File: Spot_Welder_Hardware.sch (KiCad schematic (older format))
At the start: 147 parts, among them J1 Mini USB, J2 Conn_01x03_Male, Q1 Q_NMOS_GSD, Q10 Q_NMOS_GDS, Q11 Q_NMOS_GDS, Q12 Q_NMOS_GDS, Q13 Q_NMOS_GDS, Q2 2N2219, Q3 Q_NMOS_GDS, Q4 Q_NMOS_GDS, Q5 Q_NMOS_GDS, Q6 Q_NMOS_GDS, Q7 Q_NMOS_GDS, Q8 Q_NMOS_GDS, Q9 Q_NMOS_GDS, SW1 SW_Push, SW2 SW_SPDT, SW3 Lead Voltage Trigger, SW4 SW_Push, U1 OKI, U2 ATMEGA328P, U3 FAN3122TMXCT-ND, U4 FT232RL, U5 FAN3122TMXCT-ND, Y1 Crystal

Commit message: Modified OverVoltage Protection LED
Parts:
- added R?: 10K, Resistors_SMD:R_0603_HandSoldering, symbol Device:R
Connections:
- wire segments 324 -> 328
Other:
- moved on the sheet: D11
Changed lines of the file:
@@
 L Device:LED D11
 U 1 1 5B37E14A
-P 8900 3300
-F 0 "D11" H 8900 3400 50  0000 C CNN
-F 1 "Over Voltage" H 8900 3200 50  0000 C CNN
-F 2 "LEDs:LED_0603_HandSoldering" H 8900 3300 50  0001 C CNN
-F 3 "" H 8900 3300 50  0001 C CNN
-	1    8900 3300
-	0    -1   -1   0
+P 8150 2450
+F 0 "D11" H 8150 2550 50  0000 C CNN
+F 1 "Over Voltage" H 8150 2350 50  0000 C CNN
+F 2 "LEDs:LED_0603_HandSoldering" H 8150 2450 50  0001 C CNN
+F 3 "" H 8150 2450 50  0001 C CNN
+	1    8150 2450
+	-1   0    0    1
 $EndComp
 Text Notes 6850 2600 0    24   ~ 0
@@
 	9000 2700 8900 2700
 Wire Wire Line
-	9300 3450 8900 3450
-Wire Wire Line
 	8200 3100 8150 3100
 Wire Wire Line
 	8150 3100 8150 3450
 Connection ~ 8150 3450
-Connection ~ 8900 3450
 Text Label 14350 5750 0    60   ~ 0
 DTR
@@
 	8150 3450 7800 3450
 Wire Wire Line
-	8900 3450 8150 3450
-Wire Wire Line
 	7950 3850 7950 3700
 Wire Wire Line
@@
 Text GLabel 5600 5750 0    60   Input ~ 0
 +5V
+$Comp
+L Device:R R?
+U 1 1 5BB1B4E9
+P 8650 2450
+F 0 "R?" V 8730 2450 50  0000 C CNN
+F 1 "10K" V 8650 2450 50  0000 C CNN
+F 2 "Resistors_SMD:R_0603_HandSoldering" V 8580 2450 50  0001 C CNN
+F 3 "" H 8650 2450 50  0001 C CNN
+	1    8650 2450
+	0    1    1    0
+$EndComp
+Wire Wire Line
+	8900 2600 8900 2450
+Wire Wire Line
+	8900 2450 8800 2450
+Wire Wire Line
+	8150 3450 9300 3450
+Connection ~ 8900 2600
+Wire Wire Line
+	8500 2450 8300 2450
+Wire Wire Line
+	8000 2450 7850 2450
+Wire Wire Line
+	7850 2450 7850 2600
 $EndSCHEMATC

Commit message: Swapped main MOSFETs to PSMN1R1-30PL
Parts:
- Q10, Q11, Q12, Q13, Q4, Q5, Q6, Q7, Q8, Q9: Part Number PSMN2R0-30PL -> PSMN1R1
- gave numbers to parts that had none: 1
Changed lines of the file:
@@
 F 2 "TO_SOT_Packages_THT:TO-220-3_Vertical" H 10650 2850 50  0001 C CNN
 F 3 "" H 10450 2750 50  0001 C CNN
-F 4 "PSMN2R0-30PL" H 10450 2750 60  0001 C CNN "Part Number"
+F 4 "PSMN1R1" H 10450 2750 60  0001 C CNN "Part Number"
 	1    10450 2750
-	1    0    0    -1
-$EndComp
-$Comp
-L Device:Q_NMOS_GDS Q5
-U 1 1 5B2DEBF2
-P 10950 2750
-F 0 "Q5" H 11150 2800 50  0000 L CNN
-F 1 "Q_NMOS_GDS" H 11150 2700 50  0001 L CNN
-F 2 "TO_SOT_Packages_THT:TO-220-3_Vertical" H 11150 2850 50  0001 C CNN
-F 3 "" H 10950 2750 50  0001 C CNN
-F 4 "PSMN2R0-30PL" H 10950 2750 60  0001 C CNN "Part Number"
-	1    10950 2750
-	1    0    0    -1
-$EndComp
-$Comp
-L Device:Q_NMOS_GDS Q6
-U 1 1 5B2DED1C
-P 11450 2750
-F 0 "Q6" H 11650 2800 50  0000 L CNN
-F 1 "Q_NMOS_GDS" H 11650 2700 50  0001 L CNN
-F 2 "TO_SOT_Packages_THT:TO-220-3_Vertical" H 11650 2850 50  0001 C CNN
-F 3 "" H 11450 2750 50  0001 C CNN
-F 4 "PSMN2R0-30PL" H 11450 2750 60  0001 C CNN "Part Number"
-	1    11450 2750
-	1    0    0    -1
-$EndComp
-$Comp
-L Device:Q_NMOS_GDS Q7
-U 1 1 5B2DEDBF
-P 11950 2750
-F 0 "Q7" H 12150 2800 50  0000 L CNN
-F 1 "Q_NMOS_GDS" H 12150 2700 50  0001 L CNN
-F 2 "TO_SOT_Packages_THT:TO-220-3_Vertical" H 12150 2850 50  0001 C CNN
-F 3 "" H 11950 2750 50  0001 C CNN
-F 4 "PSMN2R0-30PL" H 11950 2750 60  0001 C CNN "Part Number"
-	1    11950 2750
-	1    0    0    -1
-$EndComp
-$Comp
-L Device:Q_NMOS_GDS Q8
-U 1 1 5B2DEEC5
-P 12450 2750
-F 0 "Q8" H 12650 2800 50  0000 L CNN
-F 1 "Q_NMOS_GDS" H 12650 2700 50  0001 L CNN
-F 2 "TO_SOT_Packages_THT:TO-220-3_Vertical" H 12650 2850 50  0001 C CNN
-F 3 "" H 12450 2750 50  0001 C CNN
-F 4 "PSMN2R0-30PL" H 12450 2750 60  0001 C CNN "Part Number"
-	1    12450 2750
-	1    0    0    -1
-$EndComp
-$Comp
-L Device:Q_NMOS_GDS Q9
-U 1 1 5B2DF0C1
-P 12950 2750
-F 0 "Q9" H 13150 2800 50  0000 L CNN
-F 1 "Q_NMOS_GDS" H 13150 2700 50  0001 L CNN
-F 2 "TO_SOT_Packages_THT:TO-220-3_Vertical" H 13150 2850 50  0001 C CNN
-F 3 "" H 12950 2750 50  0001 C CNN
-F 4 "PSMN2R0-30PL" H 12950 2750 60  0001 C CNN "Part Number"
-	1    12950 2750
-	1    0    0    -1
-$EndComp
-$Comp
-L Device:Q_NMOS_GDS Q10
-U 1 1 5B2DF0C8
-P 13450 2750
-F 0 "Q10" H 13650 2800 50  0000 L CNN
-F 1 "Q_NMOS_GDS" H 13650 2700 50  0001 L CNN
-F 2 "TO_SOT_Packages_THT:TO-220-3_Vertical" H 13650 2850 50  0001 C CNN
-F 3 "" H 13450 2750 50  0001 C CNN
-F 4 "PSMN2R0-30PL" H 13450 2750 60  0001 C CNN "Part Number"
-	1    13450 2750
-	1    0    0    -1
-$EndComp
-$Comp
-L Device:Q_NMOS_GDS Q11
-U 1 1 5B2DF0CF
-P 13950 2750
-F 0 "Q11" H 14150 2800 50  0000 L CNN
-F 1 "Q_NMOS_GDS" H 14150 2700 50  0001 L CNN
-F 2 "TO_SOT_Packages_THT:TO-220-3_Vertical" H 14150 2850 50  0001 C CNN
-F 3 "" H 13950 2750 50  0001 C CNN
-F 4 "PSMN2R0-30PL" H 13950 2750 60  0001 C CNN "Part Number"
-	1    13950 2750
-	1    0    0    -1
-$EndComp
-$Comp
-L Device:Q_NMOS_GDS Q12
-U 1 1 5B2DF0D6
-P 14450 2750
-F 0 "Q12" H 14650 2800 50  0000 L CNN
-F 1 "Q_NMOS_GDS" H 14650 2700 50  0001 L CNN
-F 2 "TO_SOT_Packages_THT:TO-220-3_Vertical" H 14650 2850 50  0001 C CNN
-F 3 "" H 14450 2750 50  0001 C CNN
-F 4 "PSMN2R0-30PL" H 14450 2750 60  0001 C CNN "Part Number"
-	1    14450 2750
-	1    0    0    -1
-$EndComp
-$Comp
-L Device:Q_NMOS_GDS Q13
-U 1 1 5B2DF0DD
-P 14950 2750
-F 0 "Q13" H 15150 2800 50  0000 L CNN
-F 1 "Q_NMOS_GDS" H 15150 2700 50  0001 L CNN
-F 2 "TO_SOT_Packages_THT:TO-220-3_Vertical" H 15150 2850 50  0001 C CNN
-F 3 "" H 14950 2750 50  0001 C CNN
-F 4 "PSMN2R0-30PL" H 14950 2750 60  0001 C CNN "Part Number"
-	1    14950 2750
 	1    0    0    -1
 $EndComp
@@
 Connection ~ 10550 2950
 Connection ~ 10550 2550
-Connection ~ 14550 2550
-Connection ~ 14050 2550
-Connection ~ 13550 2550
-Connection ~ 13050 2550
-Connection ~ 12550 2550
-Connection ~ 12050 2550
-Connection ~ 11550 2550
-Connection ~ 11050 2550
-Connection ~ 11050 2950
-Connection ~ 11550 2950
-Connection ~ 12050 2950
-Connection ~ 12550 2950
-Connection ~ 13050 2950
-Connection ~ 13550 2950
-Connection ~ 14050 2950
-Connection ~ 14550 2950
 Connection ~ 14250 3700
 Connection ~ 13750 3700
@@
 	10800 2250 11800 2250
 Wire Wire Line
-	10550 2950 11050 2950
-Wire Wire Line
 	10550 2550 10800 2550
 Wire Wire Line
-	14550 2550 14800 2550
-Wire Wire Line
-	14050 2550 14550 2550
-Wire Wire Line
-	13550 2550 13800 2550
-Wire Wire Line
-	13050 2550 13550 2550
-Wire Wire Line
-	12550 2550 12800 2550
-Wire Wire Line
-	12050 2550 12550 2550
-Wire Wire Line
-	11550 2550 11800 2550
-Wire Wire Line
-	11050 2550 11550 2550
-Wire Wire Line
-	11050 2950 11550 2950
-Wire Wire Line
-	11550 2950 12050 2950
-Wire Wire Line
-	12050 2950 12550 2950
-Wire Wire Line
-	12550 2950 13050 2950
-Wire Wire Line
-	13050 2950 13550 2950
-Wire Wire Line
-	13550 2950 14050 2950
-Wire Wire Line
-	14050 2950 14550 2950
-Wire Wire Line
-	14550 2950 15050 2950
-Wire Wire Line
 	14250 3700 14750 3700
 Wire Wire Line
@@
 Wire Wire Line
 	4000 3850 4200 3850
-Wire Wire Line
-	10800 2550 11050 2550
-Wire Wire Line
-	11800 2550 12050 2550
-Wire Wire Line
-	12800 2550 13050 2550
-Wire Wire Line
-	13800 2550 14050 2550
 Wire Wire Line
 	14800 2550 15050 2550
@@
 +5V
 $Comp
-L Device:R R?
+L Device:R R40
 U 1 1 5BB1B4E9
 P 8650 2450
-F 0 "R?" V 8730 2450 50  0000 C CNN
+F 0 "R40" V 8730 2450 50  0000 C CNN
 F 1 "10K" V 8650 2450 50  0000 C CNN
 F 2 "Resistors_SMD:R_0603_HandSoldering" V 8580 2450 50  0001 C CNN
@@
 Wire Wire Line
 	7850 2450 7850 2600
+Wire Wire Line
+	13800 2550 14050 2550
+Wire Wire Line
+	12800 2550 13050 2550
+Wire Wire Line
+	11800 2550 12050 2550
+Wire Wire Line
+	10800 2550 11050 2550
+Wire Wire Line
+	10550 2950 11050 2950
+$Comp
+L Device:Q_NMOS_GDS Q5
+U 1 1 5BBA7D9A
+P 10950 2750
+F 0 "Q5" H 11150 2800 50  0000 L CNN
+F 1 "Q_NMOS_GDS" H 11150 2700 50  0001 L CNN
+F 2 "TO_SOT_Packages_THT:TO-220-3_Vertical" H 11150 2850 50  0001 C CNN
+F 3 "" H 10950 2750 50  0001 C CNN
+F 4 "PSMN1R1" H 10950 2750 60  0001 C CNN "Part Number"
+	1    10950 2750
+	1    0    0    -1
+$EndComp
+Connection ~ 11050 2550
+Wire Wire Line
+	11050 2550 11550 2550
+Connection ~ 11050 2950
+Wire Wire Line
+	11050 2950 11550 2950
+$Comp
+L Device:Q_NMOS_GDS Q6
+U 1 1 5BBA7ECA
+P 11450 2750
+F 0 "Q6" H 11650 2800 50  0000 L CNN
+F 1 "Q_NMOS_GDS" H 11650 2700 50  0001 L CNN
+F 2 "TO_SOT_Packages_THT:TO-220-3_Vertical" H 11650 2850 50  0001 C CNN
+F 3 "" H 11450 2750 50  0001 C CNN
+F 4 "PSMN1R1" H 11450 2750 60  0001 C CNN "Part Number"
+	1    11450 2750
+	1    0    0    -1
+$EndComp
+Connection ~ 11550 2550
+Wire Wire Line
+	11550 2550 11800 2550
+Connection ~ 11550 2950
+Wire Wire Line
+	11550 2950 12050 2950
+$Comp
+L Device:Q_NMOS_GDS Q7
+U 1 1 5BBA8000
+P 11950 2750
+F 0 "Q7" H 12150 2800 50  0000 L CNN
+F 1 "Q_NMOS_GDS" H 12150 2700 50  0001 L CNN
+F 2 "TO_SOT_Packages_THT:TO-220-3_Vertical" H 12150 2850 50  0001 C CNN
+F 3 "" H 11950 2750 50  0001 C CNN
+F 4 "PSMN1R1" H 11950 2750 60  0001 C CNN "Part Number"
+	1    11950 2750
+	1    0    0    -1
+$EndComp
+Connection ~ 12050 2550
+Wire Wire Line
+	12050 2550 12550 2550
+Connection ~ 12050 2950
+Wire Wire Line
+	12050 2950 12550 2950
+$Comp
+L Device:Q_NMOS_GDS Q8
+U 1 1 5BBA8134
+P 12450 2750
+F 0 "Q8" H 12650 2800 50  0000 L CNN
+F 1 "Q_NMOS_GDS" H 12650 2700 50  0001 L CNN
+F 2 "TO_SOT_Packages_THT:TO-220-3_Vertical" H 12650 2850 50  0001 C CNN
+F 3 "" H 12450 2750 50  0001 C CNN
+F 4 "PSMN1R1" H 12450 2750 60  0001 C CNN "Part Number"
+	1    12450 2750
+	1    0    0    -1
+$EndComp
+Connection ~ 12550 2550
+Wire Wire Line
+	12550 2550 12800 2550
+Connection ~ 12550 2950
+Wire Wire Line
+	12550 2950 13050 2950
+$Comp
+L Device:Q_NMOS_GDS Q9
+U 1 1 5BBA826C
+P 12950 2750
+F 0 "Q9" H 13150 2800 50  0000 L CNN
+F 1 "Q_NMOS_GDS" H 13150 2700 50  0001 L CNN
+F 2 "TO_SOT_Packages_THT:TO-220-3_Vertical" H 13150 2850 50  0001 C CNN
+F 3 "" H 12950 2750 50  0001 C CNN
+F 4 "PSMN1R1" H 12950 2750 60  0001 C CNN "Part Number"
+	1    12950 2750
+	1    0    0    -1
+$EndComp
+Connection ~ 13050 2550
+Wire Wire Line
+	13050 2550 13550 2550
+Connection ~ 13050 2950
+Wire Wire Line
+	13050 2950 13550 2950
+$Comp
+L Device:Q_NMOS_GDS Q10
+U 1 1 5BBA83A4
+P 13450 2750
+F 0 "Q10" H 13650 2800 50  0000 L CNN
+F 1 "Q_NMOS_GDS" H 13650 2700 50  0001 L CNN
+F 2 "TO_SOT_Packages_THT:TO-220-3_Vertical" H 13650 2850 50  0001 C CNN
+F 3 "" H 13450 2750 50  0001 C CNN
+F 4 "PSMN1R1" H 13450 2750 60  0001 C CNN "Part Number"
+	1    13450 2750
+	1    0    0    -1
+$EndComp
+Connection ~ 13550 2550
+Wire Wire Line
+	13550 2550 13800 2550
+Connection ~ 13550 2950
+Wire Wire Line
+	13550 2950 14050 2950
+$Comp
+L Device:Q_NMOS_GDS Q11
+U 1 1 5BBA84E2
+P 13950 2750
+F 0 "Q11" H 14150 2800 50  0000 L CNN
+F 1 "Q_NMOS_GDS" H 14150 2700 50  0001 L CNN
+F 2 "TO_SOT_Packages_THT:TO-220-3_Vertical" H 14150 2850 50  0001 C CNN
+F 3 "" H 13950 2750 50  0001 C CNN
+F 4 "PSMN1R1" H 13950 2750 60  0001 C CNN "Part Number"
+	1    13950 2750
+	1    0    0    -1
+$EndComp
+Connection ~ 14050 2550
+Wire Wire Line
+	14050 2550 14550 2550
+Connection ~ 14050 2950
+Wire Wire Line
+	14050 2950 14550 2950
+$Comp
+L Device:Q_NMOS_GDS Q12
+U 1 1 5BBA8620
+P 14450 2750
+F 0 "Q12" H 14650 2800 50  0000 L CNN
+F 1 "Q_NMOS_GDS" H 14650 2700 50  0001 L CNN
+F 2 "TO_SOT_Packages_THT:TO-220-3_Vertical" H 14650 2850 50  0001 C CNN
+F 3 "" H 14450 2750 50  0001 C CNN
+F 4 "PSMN1R1" H 14450 2750 60  0001 C CNN "Part Number"
+	1    14450 2750
+	1    0    0    -1
+$EndComp
+Connection ~ 14550 2550
+Wire Wire Line
+	14550 2550 14800 2550
+Connection ~ 14550 2950
+Wire Wire Line
+	14550 2950 15050 2950
+$Comp
+L Device:Q_NMOS_GDS Q13
+U 1 1 5BBA8762
+P 14950 2750
+F 0 "Q13" H 15150 2800 50  0000 L CNN
+F 1 "Q_NMOS_GDS" H 15150 2700 50  0001 L CNN
+F 2 "TO_SOT_Packages_THT:TO-220-3_Vertical" H 15150 2850 50  0001 C CNN
+F 3 "" H 14950 2750 50  0001 C CNN
+F 4 "PSMN1R1" H 14950 2750 60  0001 C CNN "Part Number"
+	1    14950 2750
+	1    0    0    -1
+$EndComp
 $EndSCHEMATC

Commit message: Modified Analog limiter circuit for analogue reads
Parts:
- removed D8: 5V, Diodes_SMD:D_SOD-123, symbol Device:D_Zener
- removed Q3: Q_NMOS_GDS, TO_SOT_Packages_THT:TO-220-3_Vertical, symbol Device:Q_NMOS_GDS
- added D?: 5V, Diodes_SMD:D_SOD-123, symbol Device:D_Zener
- added Q?: Q_NMOS_GDS, TO_SOT_Packages_THT:TO-220-3_Vertical, symbol Device:Q_NMOS_GDS
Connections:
- wire segments 328 -> 324
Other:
- moved on the sheet: D9, R10, R11, R15, R16
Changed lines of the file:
@@
 Text Notes 5900 6500 0    60   ~ 0
 Capacitor Voltage Read
-Text GLabel 5950 6600 0    60   Input ~ 0
+Text GLabel 6200 6950 0    60   Input ~ 0
 V+
 $Comp
 L Device:R R15
 U 1 1 5B339706
-P 6100 6600
-F 0 "R15" V 6180 6600 50  0000 C CNN
-F 1 "3000" V 6100 6600 50  0000 C CNN
-F 2 "Resistors_SMD:R_0603_HandSoldering" V 6030 6600 50  0001 C CNN
-F 3 "" H 6100 6600 50  0001 C CNN
-	1    6100 6600
+P 6350 6950
+F 0 "R15" V 6430 6950 50  0000 C CNN
+F 1 "3000" V 6350 6950 50  0000 C CNN
+F 2 "Resistors_SMD:R_0603_HandSoldering" V 6280 6950 50  0001 C CNN
+F 3 "" H 6350 6950 50  0001 C CNN
+	1    6350 6950
 	0    1    1    0
 $EndComp
@@
 L Device:R R16
 U 1 1 5B339851
-P 6300 6800
-F 0 "R16" V 6380 6800 50  0000 C CNN
-F 1 "1000" V 6300 6800 50  0000 C CNN
-F 2 "Resistors_SMD:R_0603_HandSoldering" V 6230 6800 50  0001 C CNN
-F 3 "" H 6300 6800 50  0001 C CNN
-	1    6300 6800
-	1    0    0    -1
-$EndComp
-Text GLabel 5950 7050 0    60   UnSpc ~ 0
+P 6550 7150
+F 0 "R16" V 6630 7150 50  0000 C CNN
+F 1 "1000" V 6550 7150 50  0000 C CNN
+F 2 "Resistors_SMD:R_0603_HandSoldering" V 6480 7150 50  0001 C CNN
+F 3 "" H 6550 7150 50  0001 C CNN
+	1    6550 7150
+	1    0    0    -1
+$EndComp
+Text GLabel 6200 7400 0    60   UnSpc ~ 0
 GND
-Text GLabel 6800 6650 3    60   Output ~ 0
+Text GLabel 6750 7000 3    60   Output ~ 0
 V_Sense
 $Comp
 L Device:D_Zener D9
 U 1 1 5B33E128
-P 6600 6800
-F 0 "D9" H 6600 6900 50  0000 C CNN
-F 1 "5V" H 6600 6700 50  0000 C CNN
-F 2 "Diodes_SMD:D_SOD-123" H 6600 6800 50  0001 C CNN
-F 3 "" H 6600 6800 50  0001 C CNN
-F 4 "BZT52C5V1-FDICT-ND" H 6600 6800 60  0001 C CNN "Part Number"
-	1    6600 6800
-	0    1    1    0
+P 6350 6700
+F 0 "D9" H 6350 6800 50  0000 C CNN
+F 1 "5V" H 6350 6600 50  0000 C CNN
+F 2 "Diodes_SMD:D_SOD-123" H 6350 6700 50  0001 C CNN
+F 3 "" H 6350 6700 50  0001 C CNN
+F 4 "BZT52C5V1-FDICT-ND" H 6350 6700 60  0001 C CNN "Part Number"
+	1    6350 6700
+	1    0    0    -1
 $EndComp
 Text GLabel 2250 6200 0    60   Input ~ 0
@@
 	1    0    0    -1
 $EndComp
-Text Notes 4700 6500 0    60   ~ 0
+Text Notes 4500 6500 0    60   ~ 0
 Lead Voltage Read
-Text GLabel 4500 6600 0    60   Input ~ 0
+Text GLabel 4600 6950 0    60   Input ~ 0
 VS
 $Comp
 L Device:R R10
 U 1 1 5B36668A
-P 4650 6600
-F 0 "R10" V 4730 6600 50  0000 C CNN
-F 1 "3000" V 4650 6600 50  0000 C CNN
-F 2 "Resistors_SMD:R_0603_HandSoldering" V 4580 6600 50  0001 C CNN
-F 3 "" H 4650 6600 50  0001 C CNN
-	1    4650 6600
+P 4750 6950
+F 0 "R10" V 4830 6950 50  0000 C CNN
+F 1 "3000" V 4750 6950 50  0000 C CNN
+F 2 "Resistors_SMD:R_0603_HandSoldering" V 4680 6950 50  0001 C CNN
+F 3 "" H 4750 6950 50  0001 C CNN
+	1    4750 6950
 	0    1    1    0
 $EndComp
@@
 L Device:R R11
 U 1 1 5B366690
-P 4850 6800
-F 0 "R11" V 4930 6800 50  0000 C CNN
-F 1 "1000" V 4850 6800 50  0000 C CNN
-F 2 "Resistors_SMD:R_0603_HandSoldering" V 4780 6800 50  0001 C CNN
-F 3 "" H 4850 6800 50  0001 C CNN
-	1    4850 6800
-	1    0    0    -1
-$EndComp
-Text GLabel 4500 7050 0    60   UnSpc ~ 0
+P 4950 7150
+F 0 "R11" V 5030 7150 50  0000 C CNN
+F 1 "1000" V 4950 7150 50  0000 C CNN
+F 2 "Resistors_SMD:R_0603_HandSoldering" V 4880 7150 50  0001 C CNN
+F 3 "" H 4950 7150 50  0001 C CNN
+	1    4950 7150
+	1    0    0    -1
+$EndComp
+Text GLabel 4600 7400 0    60   UnSpc ~ 0
 GND
-Text GLabel 5350 6650 3    60   Output ~ 0
+Text GLabel 5150 7000 3    60   Output ~ 0
 Lead_Sense
-$Comp
-L Device:D_Zener D8
-U 1 1 5B36669B
-P 5150 6800
-F 0 "D8" H 5150 6900 50  0000 C CNN
-F 1 "5V" H 5150 6700 50  0000 C CNN
-F 2 "Diodes_SMD:D_SOD-123" H 5150 6800 50  0001 C CNN
-F 3 "" H 5150 6800 50  0001 C CNN
-F 4 "BZT52C5V1-FDICT-ND" H 5150 6800 60  0001 C CNN "Part Number"
-	1    5150 6800
-	0    1    1    0
-$EndComp
 $Comp
 L Device:R R27
@@
 Wire Wire Line
 	2150 2400 2350 2400
-Connection ~ 4850 7050
-Wire Wire Line
-	4500 7050 4850 7050
-Wire Wire Line
-	4850 6950 4850 7050
-Wire Wire Line
-	5150 7050 5150 6950
-Connection ~ 5150 6600
-Wire Wire Line
-	5150 6600 5150 6650
-Connection ~ 4850 6600
-Wire Wire Line
-	4800 6600 4850 6600
-Wire Wire Line
-	4850 6650 4850 6600
+Wire Wire Line
+	4600 7400 4950 7400
+Wire Wire Line
+	4950 7300 4950 7400
+Wire Wire Line
+	4900 6950 4950 6950
+Wire Wire Line
+	4950 7000 4950 6950
 Connection ~ 8200 4450
 Connection ~ 8200 3850
@@
 Wire Wire Line
 	2300 6200 2300 6250
-Connection ~ 6300 7050
-Wire Wire Line
-	5950 7050 6300 7050
-Wire Wire Line
-	6300 6950 6300 7050
-Wire Wire Line
-	6600 7050 6600 6950
-Connection ~ 6600 6600
-Wire Wire Line
-	6600 6600 6600 6650
-Connection ~ 6300 6600
-Wire Wire Line
-	6250 6600 6300 6600
-Wire Wire Line
-	6300 6650 6300 6600
+Wire Wire Line
+	6200 7400 6550 7400
+Wire Wire Line
+	6550 7300 6550 7400
+Wire Wire Line
+	6500 6950 6550 6950
+Wire Wire Line
+	6550 7000 6550 6950
 Wire Wire Line
 	3900 5400 3900 5500
@@
 Wire Notes Line
 	1850 7700 15300 7700
-Wire Wire Line
-	6800 6600 6800 6650
-Wire Wire Line
-	5350 6600 5350 6650
 Wire Notes Line
 	5650 6200 5650 7700
@@
 	0    1    1    0
 $EndComp
-$Comp
-L Device:Q_NMOS_GDS Q3
-U 1 1 5B3E6852
-P 9200 2950
-F 0 "Q3" H 9400 3000 50  0000 L CNN
-F 1 "Q_NMOS_GDS" H 9400 2900 50  0001 L CNN
-F 2 "TO_SOT_Packages_THT:TO-220-3_Vertical" H 9400 3050 50  0001 C CNN
-F 3 "" H 9200 2950 50  0001 C CNN
-F 4 "PSMN2R0-30PL" H 9200 2950 60  0001 C CNN "Part Number"
-	1    9200 2950
-	1    0    0    -1
-$EndComp
 Text GLabel 5700 3600 2    60   Output ~ 0
 V+
@@
 	12550 5700 12550 6250
 Wire Wire Line
-	4850 7050 5150 7050
-Wire Wire Line
-	5150 6600 5350 6600
-Wire Wire Line
-	4850 6600 5150 6600
-Wire Wire Line
 	8200 4450 9150 4450
 Wire Wire Line
 	8200 3850 8500 3850
-Wire Wire Line
-	6300 7050 6600 7050
-Wire Wire Line
-	6600 6600 6800 6600
-Wire Wire Line
-	6300 6600 6600 6600
 Wire Wire Line
 	8200 4150 8500 4150
@@
 	1    0    0    -1
 $EndComp
+$Comp
+L Device:Q_NMOS_GDS Q?
+U 1 1 5BBA9147
+P 9200 2950
+F 0 "Q?" H 9400 3000 50  0000 L CNN
+F 1 "Q_NMOS_GDS" H 9400 2900 50  0001 L CNN
+F 2 "TO_SOT_Packages_THT:TO-220-3_Vertical" H 9400 3050 50  0001 C CNN
+F 3 "" H 9200 2950 50  0001 C CNN
+F 4 "PSMN1R1" H 9200 2950 60  0001 C CNN "Part Number"
+	1    9200 2950
+	1    0    0    -1
+$EndComp
+Text GLabel 6200 6700 0    50   Input ~ 0
++5V
+Wire Wire Line
+	6550 6950 6750 6950
+Wire Wire Line
+	6750 6950 6750 7000
+Connection ~ 6550 6950
+Wire Wire Line
+	6550 6950 6550 6700
+Wire Wire Line
+	6550 6700 6500 6700
+$Comp
+L Device:D_Zener D?
+U 1 1 5BC50F38
+P 4750 6700
+F 0 "D?" H 4750 6800 50  0000 C CNN
+F 1 "5V" H 4750 6600 50  0000 C CNN
+F 2 "Diodes_SMD:D_SOD-123" H 4750 6700 50  0001 C CNN
+F 3 "" H 4750 6700 50  0001 C CNN
+F 4 "BZT52C5V1-FDICT-ND" H 4750 6700 60  0001 C CNN "Part Number"
+	1    4750 6700
+	1    0    0    -1
+$EndComp
+Text GLabel 4600 6700 0    50   Input ~ 0
++5V
+Wire Wire Line
+	4950 6950 4950 6700
+Wire Wire Line
+	4950 6700 4900 6700
+Connection ~ 4950 6950
+Wire Wire Line
+	4950 6950 5150 6950
+Wire Wire Line
+	5150 6950 5150 7000
 $EndSCHEMATC

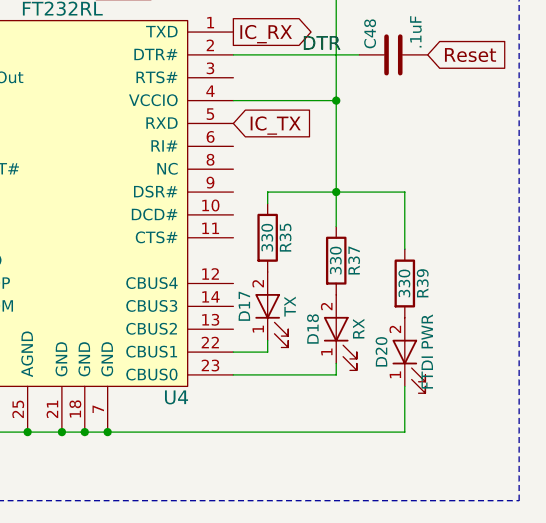
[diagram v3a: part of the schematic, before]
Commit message: Changes Resistor To 1K
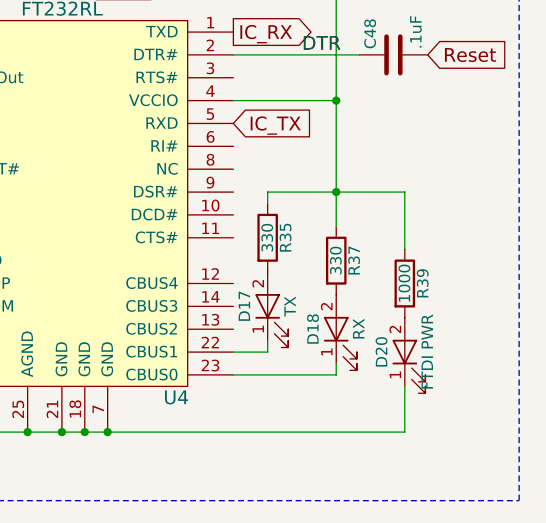
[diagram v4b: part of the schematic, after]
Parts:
- R39: value 330 -> 1000
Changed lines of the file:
@@
 P 14800 6750
 F 0 "R39" V 14880 6750 50  0000 C CNN
-F 1 "330" V 14800 6750 50  0000 C CNN
+F 1 "1000" V 14800 6750 50  0000 C CNN
 F 2 "Resistors_SMD:R_0603_HandSoldering" V 14730 6750 50  0001 C CNN
 F 3 "" H 14800 6750 50  0001 C CNN
